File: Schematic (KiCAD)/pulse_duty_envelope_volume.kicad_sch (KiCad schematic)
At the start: 72 parts, among them J65 Reg 4 D-Latch N, J68 Counter 4 Reset CL3

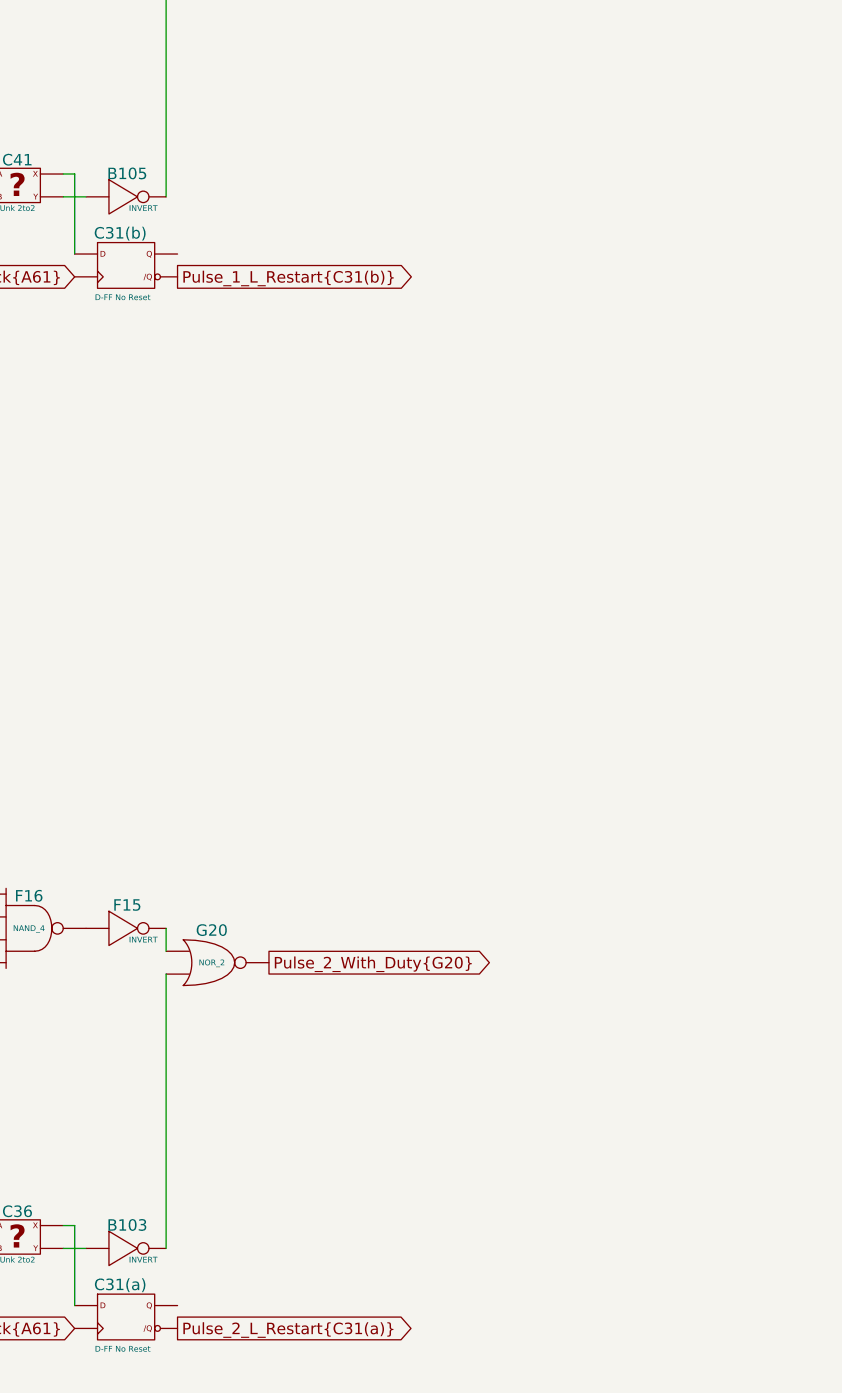
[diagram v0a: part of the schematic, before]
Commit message: - All cells in the left and center areas have now been added into the schematics.  - Changed naming of the PDF files; I was accidentally writing over furrtek's original with my new PDF.
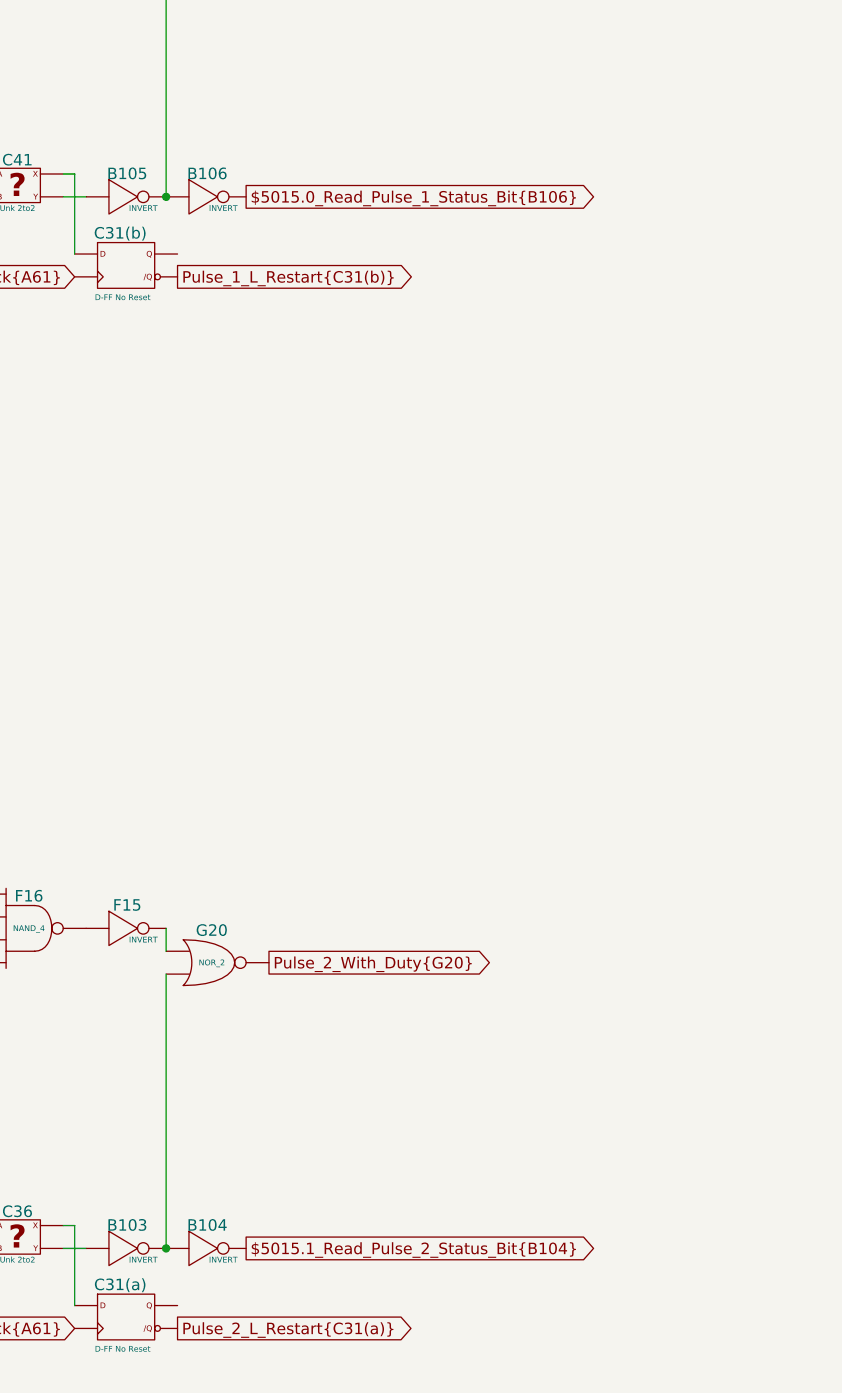
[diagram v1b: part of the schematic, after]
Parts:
- added B104, B106: INVERT, symbol MMC5:INVERT
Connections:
- net at H90. (X): now also G94. (X); no longer H89. (X)
- net at C36. (Y): now also B103. (X); no longer C34. (X)
- net at C35. (X): now also C33. (X); no longer C36. (Y)
- net at B103. (X): now also G20. (X), B104. (X); no longer C36. (Y)
- net at F36. (X): now also G97. (X); no longer F32. (X)
- net at B105. (X): now also C41. (Y); no longer F32. (X)
- net at C39. (X): now also C38. (X); no longer C41. (Y)
- net at E47. (X): now also F10. (X); no longer E48. (X)
- net at F15. (X): now also F16. (X); no longer G20. (X)
- net at G97. (X): now also G99. (X); no longer G98. (X)
- net at C41. (Y): now also C31(b). (/Q); no longer B105. (X)
- net at F16. (X): now also F13. (X); no longer F11. (X)
- new net: E45. (X), E46. (X), E47. (X), F12. (X)
- new net: F19. (X), F23. (X)
- new net: B99. (X), C38. (X)
- new net: H89. (X), H90. (X)
- new net: G99. (X), H90. (X), H91. (X), H92. (X)
- new net: C34. (X), C36. (Y)
- new net: C35. (X), C36. (Y)
- new net: C31(a). (/Q), C36. (Y)
- new net: H101. (X), H105. (X)
- new net: H100. (X), H104. (X)
- new net: F20. (X), F24. (X)
- new net: F32. (X), F36. (X)
- new net: B105. (X), B106. (X), F32. (X)
- new net: F35. (X), G85. (/Q3)
- new net: F34. (X), G85. (/Q3)
- new net: C39. (X), C41. (Y)
- new net: E47. (X), E48. (X)
- new net: F18. (X), F22. (X)
- new net: C37. (X), C38. (X)
- new net: F15. (X), G20. (X)
- new net: G97. (X), G98. (X)
- new net: C40. (X), C41. (Y)
- new net: H103. (X), H107. (X)
- new net: C32. (X), C33. (X)
- new net: H102. (X), H106. (X)
- new net: F11. (X), F16. (X)
- new net: G93. (X), G97. (X)
- new net: F21. (X), F26. (X)
- new net: E68. (/Q3), F7.1. (X)
- new net: E68. (/Q3), F8. (X)
- new net: G94. (X), G97. (X)
- new net: F10. (X), F16. (X)
- new net: F12. (X), F16. (X)
- new net: B100. (X), C33. (X)
- new net $5015.0_Read_Pulse_1_Status_Bit{B106}: B106. (X)
- new net $5015.1_Read_Pulse_2_Status_Bit{B104}: B104. (X)
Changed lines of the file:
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@@
 	)
 	(junction
+		(at 248.92 213.36)
+		(diameter 0)
+		(color 0 0 0 0)
+	)
+	(junction
 		(at 43.18 72.39)
 		(diameter 0)
@@
 		(color 0 0 0 0)
 	)
+	(junction
+		(at 248.92 96.52)
+		(diameter 0)
+		(color 0 0 0 0)
+	)
 	(wire
 		(pts
@@
 		)
 	)
+	(global_label "$5015.0_Read_Pulse_1_Status_Bit{B106}"
+		(shape output)
+		(at 257.81 96.52 0)
+		(fields_autoplaced yes)
+		(effects
+			(font
+				(size 1.27 1.27)
+			)
+			(justify left)
+		)
+		(property "Intersheetrefs" "${INTERSHEET_REFS}"
+			(at 299.7414 96.52 0)
+			(effects
+				(font
+					(size 1.27 1.27)
+				)
+				(justify left)
+				(hide yes)
+			)
+		)
+	)
 	(global_label "{slash}$5004.6_Duty.0{F8}"
 		(shape output)
@@
 		)
 	)
+	(global_label "$5015.1_Read_Pulse_2_Status_Bit{B104}"
+		(shape output)
+		(at 257.81 213.36 0)
+		(fields_autoplaced yes)
+		(effects
+			(font
+				(size 1.27 1.27)
+			)
+			(justify left)
+		)
+		(property "Intersheetrefs" "${INTERSHEET_REFS}"
+			(at 299.7414 213.36 0)
+			(effects
+				(font
+					(size 1.27 1.27)
+				)
+				(justify left)
+				(hide yes)
+			)
+		)
+	)
 	(global_label "{slash}$5000.4_Vol{slash}Env_Flag{H99}"
 		(shape input)
@@
 	)
 	(symbol
+		(lib_name "INVERT_23")
+		(lib_id "MMC5:INVERT")
+		(at 254 213.36 0)
+		(unit 1)
+		(exclude_from_sim no)
+		(in_bom yes)
+		(on_board yes)
+		(dnp no)
+		(property "Reference" "B104"
+			(at 253.492 210.058 0)
+			(do_not_autoplace yes)
+			(effects
+				(font
+					(size 1.27 1.27)
+				)
+				(justify top)
+			)
+		)
+		(property "Value" "INVERT"
+			(at 255.27 214.63 0)
+			(do_not_autoplace yes)
+			(effects
+				(font
+					(size 0.635 0.635)
+				)
+			)
+		)
+		(property "Footprint" ""
+			(at 254 213.36 0)
+			(effects
+				(font
+					(size 1.27 1.27)
+				)
+				(hide yes)
+			)
+		)
+		(property "Datasheet" ""
+			(at 254 213.36 0)
+			(effects
+				(font
+					(size 1.27 1.27)
+				)
+				(hide yes)
+			)
+		)
+		(property "Description" ""
+			(at 254 213.36 0)
+			(effects
+				(font
+					(size 1.27 1.27)
+				)
+				(hide yes)
+			)
+		)
+		(pin ""
+		)
+		(pin ""
+		)
+		(instances
+			(project "MMC5"
+				(path "/46093bf6-f83e-4237-9ece-7350a682aff0/58ac8c8e-9b19-48e1-aca9-8ec408ceb475"
+					(reference "B104")
+					(unit 1)
+				)
+			)
+		)
+	)
+	(symbol
 		(lib_name "INVERT_7")
 		(lib_id "MMC5:INVERT")
@@
 					(unit 1)
 				)
+			)
+		)
+	)
+	(symbol
+		(lib_name "INVERT_24")
+		(lib_id "MMC5:INVERT")
+		(at 254 96.52 0)
+		(unit 1)
+		(exclude_from_sim no)
+		(in_bom yes)
+		(on_board yes)
+		(dnp no)
+		(property "Reference" "B106"
+			(at 253.492 93.218 0)
+			(do_not_autoplace yes)
+			(effects
+				(font
+					(size 1.27 1.27)
+				)
+				(justify top)
+			)
+		)
+		(property "Value" "INVERT"
+			(at 255.27 97.79 0)
+			(do_not_autoplace yes)
+			(effects
+				(font
+					(size 0.635 0.635)
+				)
+			)
+		)
+		(property "Footprint" ""
+			(at 254 96.52 0)
+			(effects
+				(font
+					(size 1.27 1.27)
+				)
+				(hide yes)
+			)
+		)
+		(property "Datasheet" ""
+			(at 254 96.52 0)
+			(effects
+				(font
+					(size 1.27 1.27)
+				)
+				(hide yes)
+			)
+		)
+		(property "Description" ""
+			(at 254 96.52 0)
+			(effects
+				(font
+					(size 1.27 1.27)
+				)
+				(hide yes)
+			)
+		)
+		(pin ""
+		)
+		(pin ""
+		)
+		(instances
+			(project "MMC5"
+				(path "/46093bf6-f83e-4237-9ece-7350a682aff0/58ac8c8e-9b19-48e1-aca9-8ec408ceb475"
+					(reference "B106")
+					(unit 1)
+				)
